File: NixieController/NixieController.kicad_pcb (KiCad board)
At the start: 2 copper layers, 156.5 x 67.5 mm, 77 parts, among them J1 Conn_01x07, J10 Conn_01x06, J11 Conn_01x05, J12 Barrel_Jack, J13 Conn_01x07, J14 Conn_01x07, J15 Conn_01x07, J2 Conn_01x01, J3 Conn_01x01, J4 Conn_01x01, J5 Conn_01x01, J6 Conn_01x04, J7 Conn_01x04, J8 Conn_01x04, J9 Conn_01x04, Q1 2N2222A, Q2 2N2222A, Q3 2N2222A, SW1 SW_Push, SW2 SW_Push, SW3 SW_Push, U2 L7805

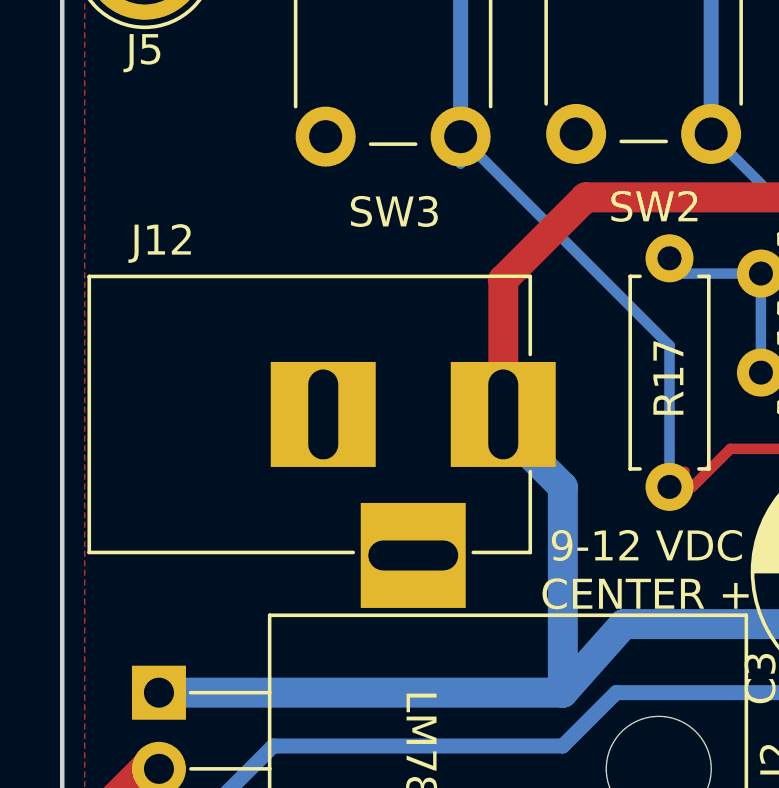
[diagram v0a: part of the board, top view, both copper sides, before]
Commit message: Placed connectors to make boards stackable
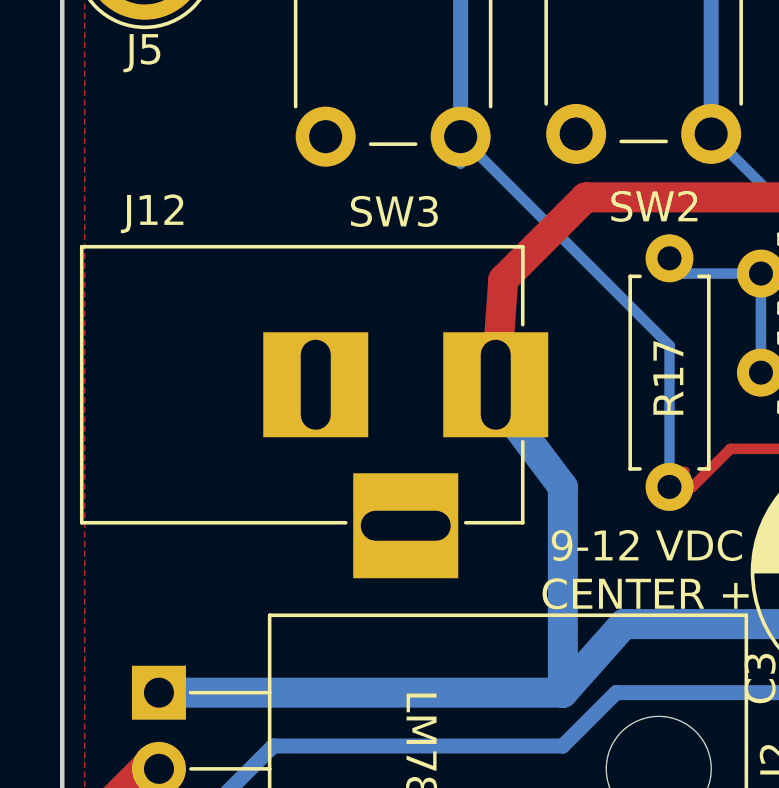
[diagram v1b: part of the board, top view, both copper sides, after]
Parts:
- moved J12 1.02 mm to (126.7, 65.8)
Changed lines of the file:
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@@
   )
   (module Connectors:BARREL_JACK (layer F.Cu)
-    (at 126.95 66.79)
+    (at 126.7 65.8)
     (descr "DC Barrel Jack")
     (tags "Power Jack")
@@
   (segment (start 137.2375 77.842) (end 137.2375 75.8905) (width 1) (layer F.Cu) (net 7))
   (segment (start 137.2375 75.8905) (end 139.35 73.778) (width 1) (layer F.Cu) (net 7))
-  (segment (start 126.95 66.79) (end 126.95 67.22) (width 1) (layer B.Cu) (net 7))
-  (segment (start 126.95 67.22) (end 128.936 69.206) (width 1) (layer B.Cu) (net 7))
+  (segment (start 126.7 65.8) (end 126.7 66.23) (width 1) (layer B.Cu) (net 7) (status 30))
+  (segment (start 126.7 66.23) (end 128.936 69.206) (width 1) (layer B.Cu) (net 7) (status 10))
   (segment (start 128.936 69.206) (end 128.936 76.064) (width 1) (layer B.Cu) (net 7))
   (segment (start 139.35 73.778) (end 133 73.778) (width 1) (layer B.Cu) (net 7))
@@
   (segment (start 139.35 59.554) (end 129.698 59.554) (width 1) (layer F.Cu) (net 7))
   (segment (start 140.366 58.538) (end 139.35 59.554) (width 1) (layer F.Cu) (net 7))
-  (segment (start 126.95 62.302) (end 126.95 66.79) (width 1) (layer F.Cu) (net 7))
+  (segment (start 126.95 62.302) (end 126.7 65.8) (width 1) (layer F.Cu) (net 7) (status 20))
   (segment (start 129.698 59.554) (end 126.95 62.302) (width 1) (layer F.Cu) (net 7))
   (segment (start 145.542 50.06) (end 150.69 50.06) (width 1) (layer F.Cu) (net 7))
@@
   (segment (start 140.366 53.712) (end 143.414 53.712) (width 1) (layer F.Cu) (net 7))
   (segment (start 177.77 50.06) (end 150.69 50.06) (width 1) (layer F.Cu) (net 7))
-  (segment (start 126.95 66.79) (end 126.95 66.94) (width 1) (layer F.Cu) (net 7))
-  (segment (start 126.95 66.94) (end 127.52 67.51) (width 1) (layer F.Cu) (net 7))
+  (segment (start 126.7 65.8) (end 126.7 65.95) (width 1) (layer F.Cu) (net 7) (status 30))
+  (segment (start 126.7 65.95) (end 127.27 66.52) (width 1) (layer F.Cu) (net 7) (status 30))
   (segment (start 137.2375 77.842) (end 137.2375 82.1875) (width 1) (layer F.Cu) (net 7))
   (segment (start 137.2375 82.1875) (end 137.2375 82.3125) (width 0.5) (layer F.Cu) (net 7))

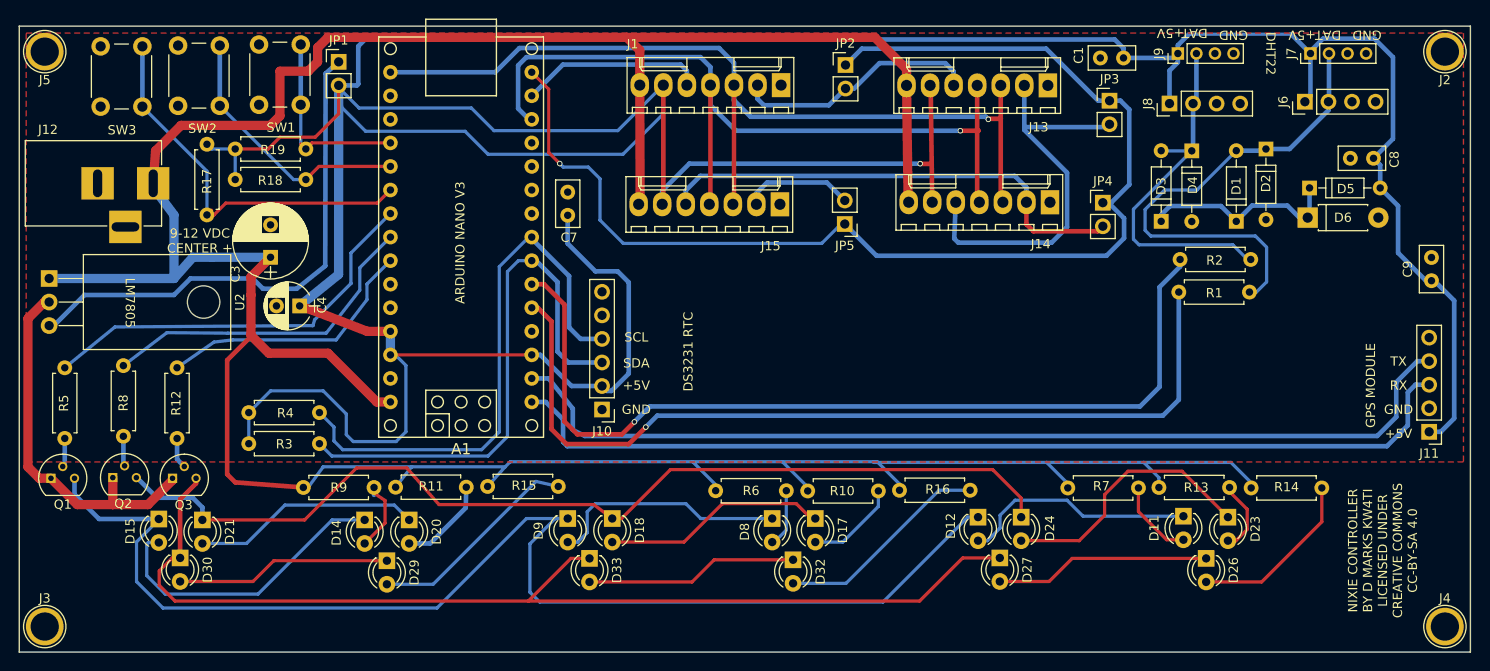
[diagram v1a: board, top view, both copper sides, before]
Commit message: First usable version of Nixie Tube Clock
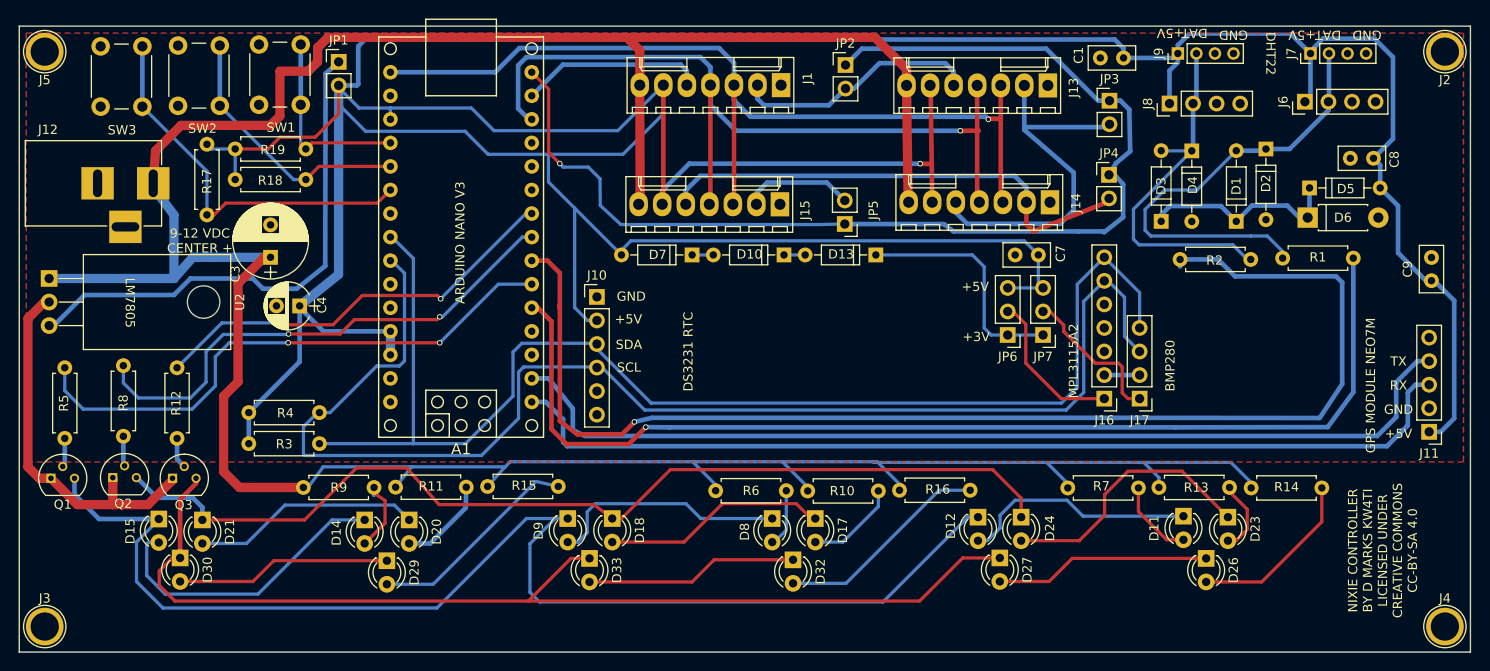
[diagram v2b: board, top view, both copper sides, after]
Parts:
- added D10: 1N4148, Diodes_THT:D_DO-35_SOD27_P7.62mm_Horizontal, F.Cu at (194.7, 73.5)
- added D13: 1N4148, Diodes_THT:D_DO-35_SOD27_P7.62mm_Horizontal, F.Cu at (204.6, 73.5)
- added D7: 1N4148, Diodes_THT:D_DO-35_SOD27_P7.62mm_Horizontal, F.Cu at (184.8, 73.5)
- added J16: Conn_01x07, Pin_Headers:Pin_Header_Straight_1x07_Pitch2.54mm, F.Cu at (229.3, 89.0)
- added J17: Conn_01x04, Pin_Headers:Pin_Header_Straight_1x04_Pitch2.54mm, F.Cu at (233.1, 89.0)
- added JP6: Jumper_NC_Dual, Pin_Headers:Pin_Header_Straight_1x03_Pitch2.54mm, F.Cu at (218.9, 82.2)
- added JP7: Jumper_NC_Dual, Pin_Headers:Pin_Header_Straight_1x03_Pitch2.54mm, F.Cu at (222.7, 82.2)
- moved C7 50.9 mm to (222.2, 73.5), turned to 180 degrees
- moved J10 12.2 mm to (174.6, 78.0), turned to 0 degrees
- moved R1 5.12 mm to (248.5, 73.9), turned to 0 degrees
- moved JP4 3.07 mm to (229.8, 64.9)
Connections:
- A1 pad 18: (no net) -> +5V
- A1 pad 22: LED1 -> (no net)
- A1 pad 23: LED2 -> SDA
- A1 pad 24: LED3 -> SCL
- A1 pad 3: +5V -> (no net)
- A1 pad 30: +12V -> (no net)
- A1 pad 6: Net-(A1-Pad6) -> LED1
- A1 pad 7: SDA -> Net-(A1-Pad7)
- A1 pad 8: SCL -> LED2
- A1 pad 9: (no net) -> LED3
- R2 pad 2: Net-(A1-Pad6) -> Net-(A1-Pad7)
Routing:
- net Net-(A1-Pad7): track 0.00 -> 138.0 mm, vias 0 -> 1
- net Net-(A1-Pad6): track 98.6 -> 0.00 mm, vias 1 -> 0
- net SCL: track 61.2 -> 145.0 mm
- net SDA: track 59.5 -> 140.5 mm
- net Net-(D13-Pad1): track 0.00 -> 25.5 mm
- net Net-(A1-Pad5): track 96.3 -> 118.6 mm
- net LED2: track 36.0 -> 56.6 mm, vias 0 -> 2
- net +5V: track 465.5 -> 483.5 mm
- net LED1: track 43.9 -> 61.1 mm, vias 0 -> 2
- net +12V: track 347.5 -> 330.5 mm
- net LED3: track 28.8 -> 45.6 mm, vias 0 -> 2
- net Net-(J16-Pad1): track 0.00 -> 16.8 mm
- net Net-(J17-Pad1): track 0.00 -> 16.4 mm
- net SERDATAOUT: track 132.1 -> 124.6 mm
- net GND: track 40.5 -> 44.3 mm
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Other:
- board text added: "+3V"
- board text added: "BMP280"
- board text added: "GPS MODULE NEO7M"
- board text added: "MPL3115A2"
- board text removed: "GPS MODULE"

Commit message: Added speaker output
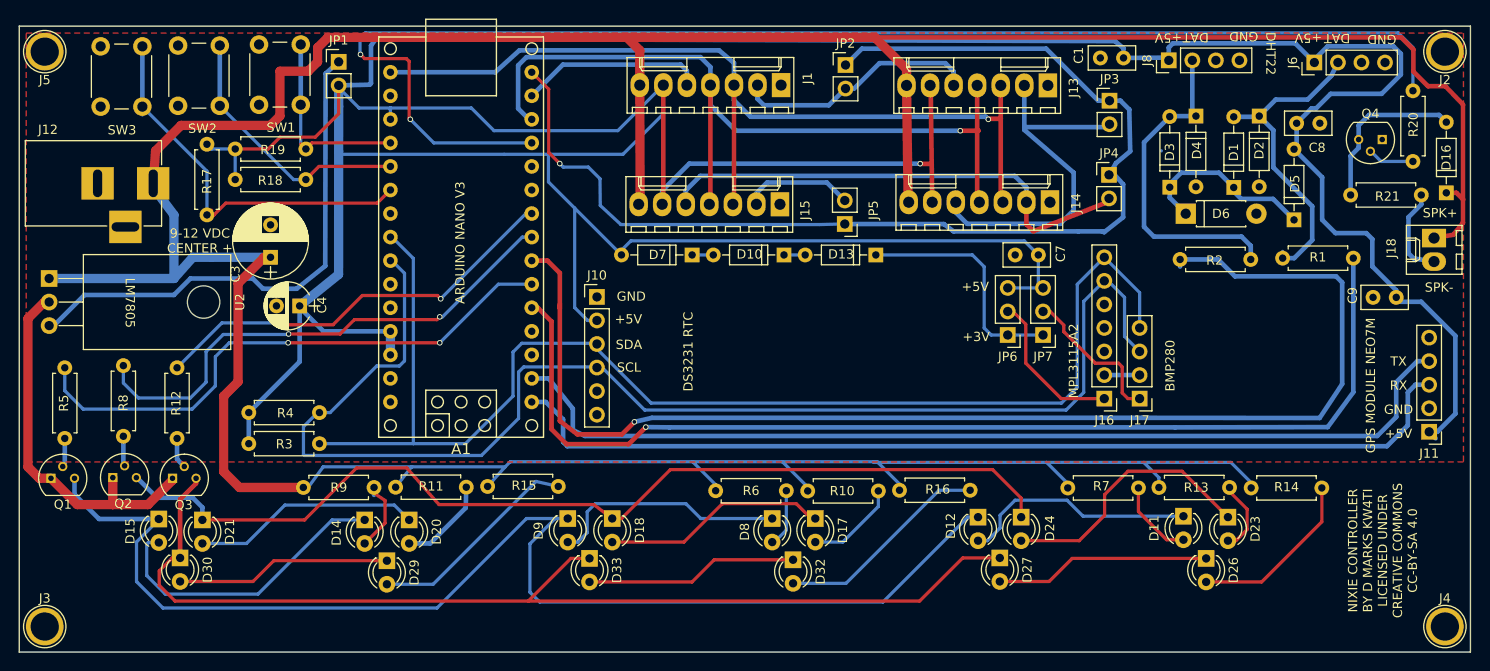
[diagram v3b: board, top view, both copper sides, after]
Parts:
- removed J7, J9: Conn_01x04, Pin_Headers:Pin_Header_Straight_1x04_Pitch2.00mm
- added D16: 1N4148, Diodes_THT:D_DO-35_SOD27_P7.62mm_Horizontal, F.Cu at (266.1, 66.8)
- added J18: Conn_01x02, Connectors_Molex:Molex_KK-6410-02_02x2.54mm_Straight, F.Cu at (264.8, 71.7)
- added Q4: 2N2222A, TO_SOT_Packages_THT:TO-92_Molded_Narrow, F.Cu at (259.2, 61.1)
- added R20: 1k, Resistors_THT:R_Axial_DIN0207_L6.3mm_D2.5mm_P7.62mm_Horizontal, F.Cu at (262.6, 55.8)
- added R21: 100R, Resistors_THT:R_Axial_DIN0207_L6.3mm_D2.5mm_P7.62mm_Horizontal, F.Cu at (263.4, 67.1)
- moved D6 13.2 mm to (238.1, 69.1)
- moved C8 9.11 mm to (250.0, 59.3), turned to 0 degrees
- moved J8 4.66 mm to (236.2, 52.5)
- moved J6 4.35 mm to (251.9, 52.8)
- moved C9 4.20 mm to (260.8, 78.1), turned to 180 degrees
- moved D5 3.82 mm to (249.7, 69.7), turned to 90 degrees
- moved D3 3.79 mm to (236.3, 66.2)
- moved D4 3.78 mm to (239.2, 58.5)
- moved D1 3.66 mm to (243.2, 66.2)
- moved D2 3.62 mm to (246.0, 58.5)
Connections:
- A1 pad 12: (no net) -> AUDIO
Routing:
- net AUDIO: track 0.00 -> 146.9 mm, vias 0 -> 2
- net +12V: track 330.5 -> 417.0 mm
- net Net-(D16-Pad2): track 0.00 -> 18.1 mm
- net SENSORDATA1: track 49.3 -> 34.5 mm
- net Net-(J18-Pad2): track 0.00 -> 9.86 mm
- net Net-(Q4-Pad2): track 0.00 -> 5.03 mm
- net SENSORDATA2: track 39.7 -> 36.6 mm
- net +5V: track 483.5 -> 486.2 mm
- net Net-(D1-Pad1): track 22.1 -> 20.2 mm
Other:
- board text added: "SPK+"
- board text added: "SPK-"

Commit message: Changed connector between boards to 10 pin IDC, added Bill of Materials
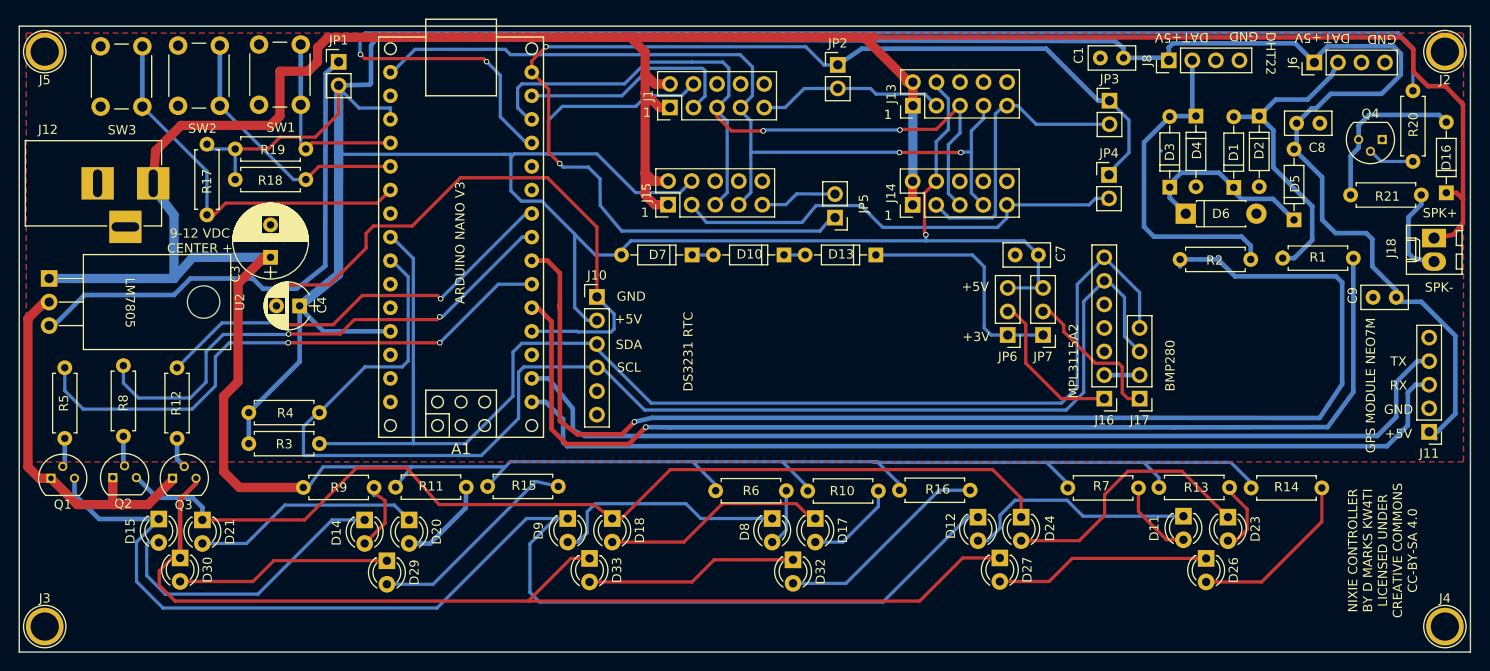
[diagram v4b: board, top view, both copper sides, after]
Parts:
- J1, J13, J14, J15: value Conn_01x07 -> Conn_02x05_Odd_Even; footprint Connectors_Molex:Molex_KK-6410-07_07x2.54mm_Straight -> Pin_Headers:Pin_Header_Straight_2x05_Pitch2.54mm
- moved J14 14.8 mm to (208.6, 68.1), turned to 90 degrees
- moved J13 14.7 mm to (208.6, 57.4), turned to 90 degrees
- moved J1 12.2 mm to (182.4, 57.6), turned to 90 degrees
- moved J15 12.1 mm to (182.2, 68.1), turned to 90 degrees
- moved JP5 1.26 mm to (200.2, 69.5)
- moved JP2 0.84 mm to (200.5, 53.0)
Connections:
- A1 pad 28: +5V -> (no net)
- J1 pad 1: GND -> +12V
- J1 pad 2: Net-(J1-Pad2) -> +12V
- J1 pad 3: SERCLK -> SERDATA
- J1 pad 4: SERLATCH -> +5V
- J1 pad 5: SERDATA -> SERLATCH
- J1 pad 6: +5V -> GND
- J1 pad 7: +12V -> SERCLK
- J13 pad 1: GND -> +12V
- J13 pad 2: Net-(J13-Pad2) -> +12V
- J13 pad 3: SERCLK -> Net-(J1-Pad9)
- J13 pad 4: SERLATCH -> +5V
- J13 pad 5: Net-(J1-Pad2) -> SERLATCH
- J13 pad 6: +5V -> GND
- J13 pad 7: +12V -> SERCLK
- J14 pad 1: GND -> +12V
- J14 pad 2: Net-(J14-Pad2) -> +12V
- J14 pad 3: SERCLK -> Net-(J13-Pad9)
- J14 pad 4: SERLATCH -> +5V
- J14 pad 5: Net-(J13-Pad2) -> SERLATCH
- J14 pad 6: +5V -> GND
- J14 pad 7: +12V -> SERCLK
- J15 pad 1: GND -> +12V
- J15 pad 2: Net-(J15-Pad2) -> +12V
- J15 pad 3: SERCLK -> Net-(J14-Pad9)
- J15 pad 4: SERLATCH -> +5V
- J15 pad 5: Net-(J14-Pad2) -> SERLATCH
- J15 pad 6: +5V -> GND
- J15 pad 7: +12V -> SERCLK
- JP2 pad 2: Net-(J1-Pad2) -> Net-(J1-Pad9)
- JP3 pad 2: Net-(J13-Pad2) -> Net-(J13-Pad9)
- JP4 pad 2: Net-(J14-Pad2) -> Net-(J14-Pad9)
- JP5 pad 2: Net-(J15-Pad2) -> Net-(J15-Pad9)
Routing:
- net GND: track 44.3 -> 109.1 mm
- net Net-(J14-Pad2): track 54.1 -> 0.00 mm
- net Net-(J14-Pad9): track 0.00 -> 50.6 mm
- net +5V: track 486.2 -> 435.7 mm
- net Net-(J13-Pad2): track 40.1 -> 0.00 mm
- net Net-(J13-Pad9): track 0.00 -> 31.9 mm
- net Net-(J1-Pad2): track 26.7 -> 0.00 mm
- net Net-(J1-Pad9): track 0.00 -> 20.2 mm
- net +12V: track 417.0 -> 431.0 mm
- net Net-(J15-Pad2): track 12.0 -> 0.00 mm
- net Net-(J15-Pad9): track 0.00 -> 8.96 mm
- net SERCLK: track 99.1 -> 93.8 mm, vias 1 -> 2
- net SERDATA: track 19.9 -> 24.5 mm
- net SERLATCH: track 88.3 -> 86.0 mm, vias 1 -> 2
- net AUDIO: track 146.9 -> 145.9 mm
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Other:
- board text added: "1"
